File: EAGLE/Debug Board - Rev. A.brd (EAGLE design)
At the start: 29.5 x 33 mm, 5 parts, among them J1 M50-3032042, J2 M50-3032042, J3 224920, J4 M50-3031042, J5 DF12NB-40DS-0.5V_51_

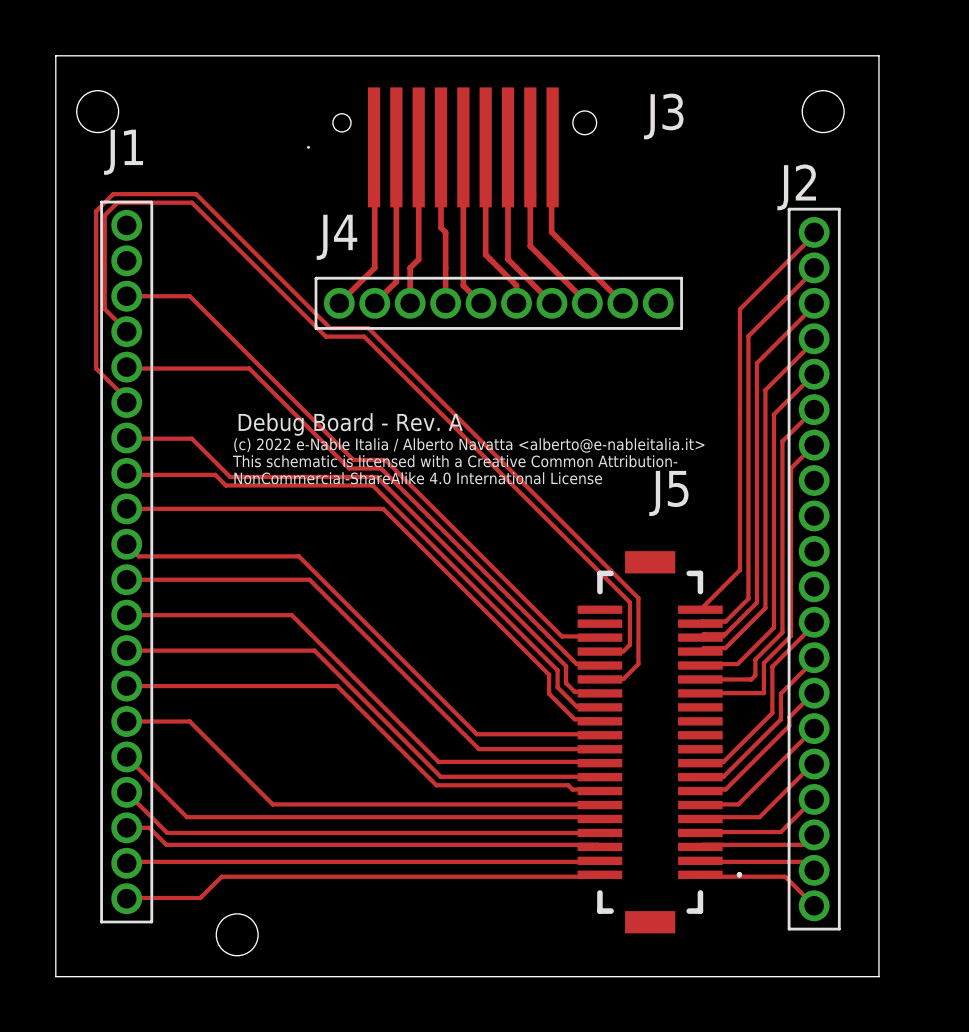
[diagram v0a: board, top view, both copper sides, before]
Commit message: Updated Debug Board to Rev. A:
Added power and data bus connector on the bottom side of the board
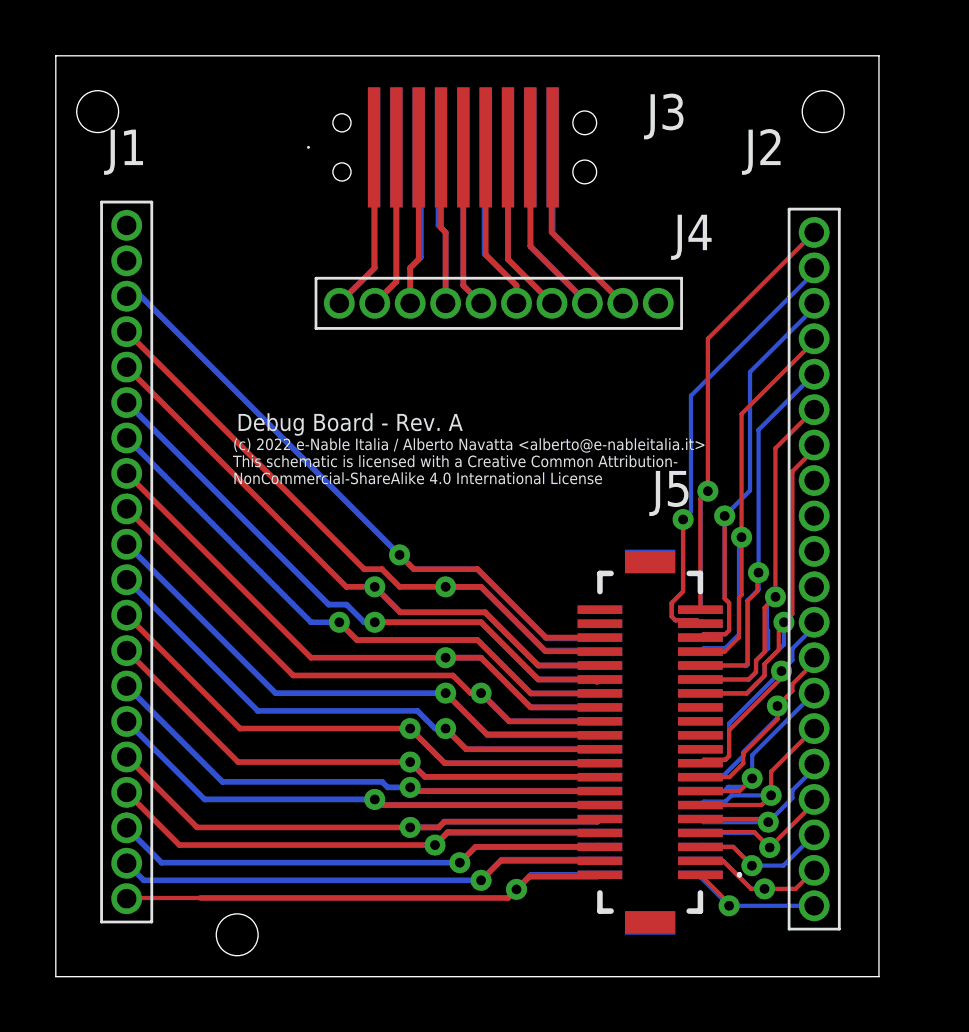
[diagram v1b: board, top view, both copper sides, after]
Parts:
- added J6: 224920, SamacSys_Parts:224920
- added J7: DF12NB_4.0_-40DP-0.5V_51_, SamacSys_Parts:DF12NB4040DP05V51
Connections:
- net +3V3-A: now also J6.4
- net +3V3-B: now also J6.5
- net +3V3-C: now also J6.6
- net +5V-A: now also J6.1
- net +5V-B: now also J6.2
- net +5V-C: now also J6.3
- net CS0: now also J7.38
- net D0: now also J7.2
- net D1: now also J7.4
- net D2: now also J7.6
- net D3: now also J7.8
- net D4: now also J7.10
- net D5: now also J7.12
- net D6: now also J7.14
- net DIN/MOSI: now also J7.36
- net DOUT/MISO: now also J7.34
- net GND: now also J7.40
- net GND-A: now also J6.7
- net GND-B: now also J6.8
- net GND-C: now also J6.9
- net IO1: now also J7.1
- net IO10: now also J7.19
- net IO11: now also J7.21
- net IO12: now also J7.23
- net IO13: now also J7.25
- net IO14: now also J7.27
- net IO15: now also J7.29
- net IO16: now also J7.31
- net IO17: now also J7.33
- net IO18: now also J7.35
- net IO2: now also J7.3
- net IO3: now also J7.5
- net IO4/SCL1: now also J7.7
- net IO5/SDA1: now also J7.9
- net IO6: now also J7.11
- net IO7: now also J7.13
- net IO8: now also J7.15
- net IO9: now also J7.17
- net RXD0/SDA0: now also J7.30
- net SCLK: now also J7.32
- net TXD0/SCL0: now also J7.28
- net USB_D+/D8: now also J7.18
- net USB_D-/D7: now also J7.16
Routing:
- net IO14: track 21.1 -> 31.2 mm, vias 0 -> 1
- net IO16: track 21.4 -> 30.7 mm, vias 0 -> 1
- net IO18: track 22.0 -> 30.5 mm, vias 0 -> 1
- net IO6: track 18.2 -> 26.4 mm, vias 0 -> 1
- net IO9: track 19.2 -> 26.6 mm, vias 0 -> 1
- net IO5/SDA1: track 17.9 -> 25.2 mm, vias 0 -> 1
- net IO8: track 18.8 -> 25.9 mm, vias 0 -> 1
- net IO7: track 18.5 -> 25.4 mm, vias 0 -> 1
- net IO15: track 37.0 -> 30.2 mm, vias 0 -> 1
- net GND-C: track 8.04 -> 14.7 mm
- net GND-B: track 7.74 -> 14.2 mm
- net IO4/SCL1: track 17.6 -> 24.0 mm, vias 0 -> 1
- net GND-A: track 6.24 -> 12.5 mm
- net IO11: track 19.8 -> 25.9 mm, vias 0 -> 1
- net +5V-A: track 6.12 -> 12.2 mm
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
